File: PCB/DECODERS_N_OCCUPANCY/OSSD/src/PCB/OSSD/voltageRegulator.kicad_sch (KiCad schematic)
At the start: 7 parts, among them U401 L78L05_SOT89

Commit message: added some files
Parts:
- renumbered D501 to D2

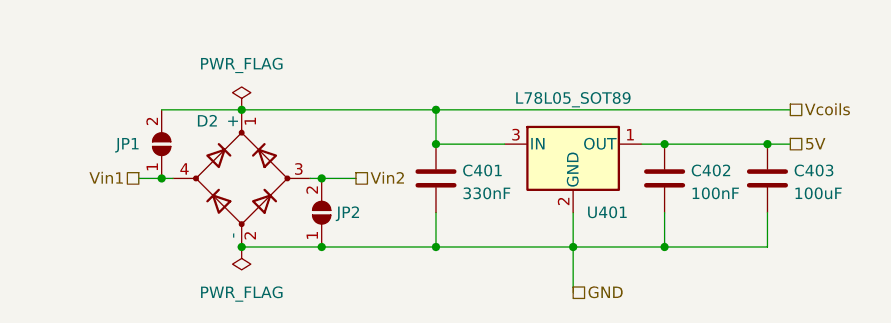
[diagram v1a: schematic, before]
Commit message: Added PDF files for all schematics
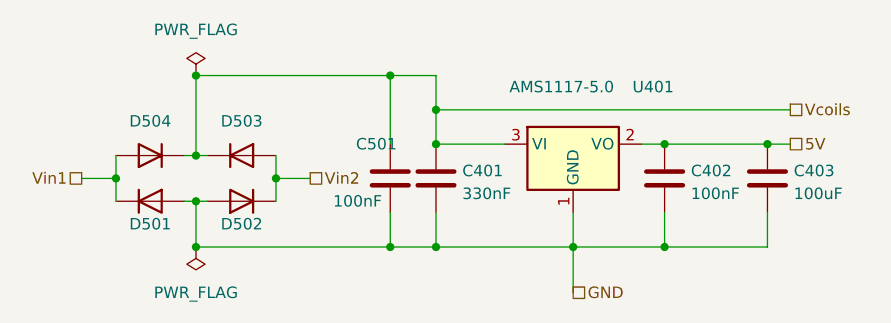
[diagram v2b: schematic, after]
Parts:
- removed D2: ~, custom_kicad_lib_sk:4A rectifier, symbol Device:D_Bridge_+-AA
- removed JP1, JP2: SolderJumper_2_Open, Jumper:SolderJumper-2_P1.3mm_Open_RoundedPad1.0x1.5mm, symbol Jumper:SolderJumper_2_Open
- removed U401: L78L05_SOT89, Package_TO_SOT_SMD:SOT-89-3, symbol Regulator_Linear:L78L05_SOT89
- added C501: 100nF, Capacitor_SMD:C_0603_1608Metric_Pad1.08x0.95mm_HandSolder, symbol Device:C
- added D501, D502, D503, D504: SS53, Diode_SMD:D_SMA, symbol custom_kicad_lib_sk:SS53
- added U401: AMS1117-5.0, Package_TO_SOT_SMD:SOT-223-3_TabPin2, symbol custom_kicad_lib_sk:AMS1117-5.0
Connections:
- net 5V: now also U401.2 (VO)
- net GND: now also C501.2, D501.2 (A), D502.2 (A), U401.1 (GND)
- net Vcoils: now also C501.1, D503.1 (K), D504.1 (K), U401.3 (VI)
- net Vin1: now also D501.1 (K), D504.2 (A)
- net Vin2: now also D502.1 (K), D503.2 (A)
